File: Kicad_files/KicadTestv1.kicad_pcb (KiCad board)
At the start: 2 copper layers, 7 parts, among them J1 Conn_01x10_MountingPin, J2 Conn_01x04, SW1 SW_Push

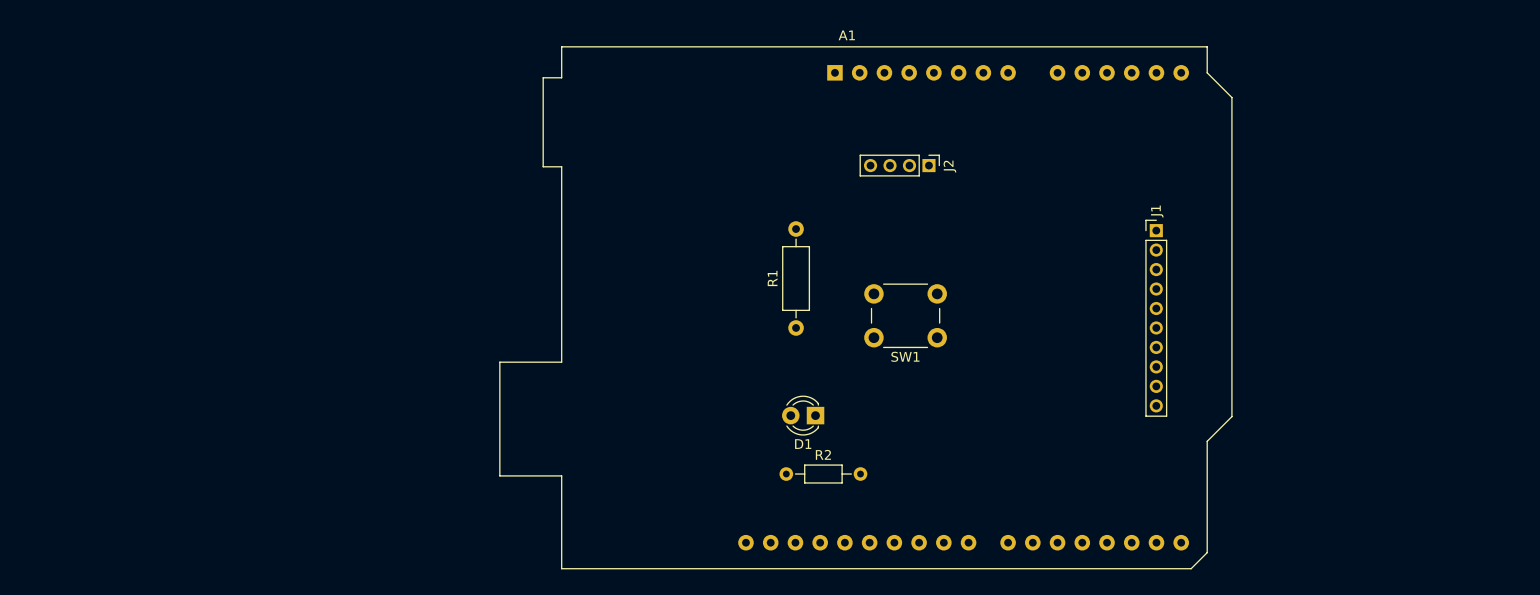
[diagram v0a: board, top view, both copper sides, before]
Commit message: Ajout Lib pour RN2483 & Modificition Empreinte et cablage
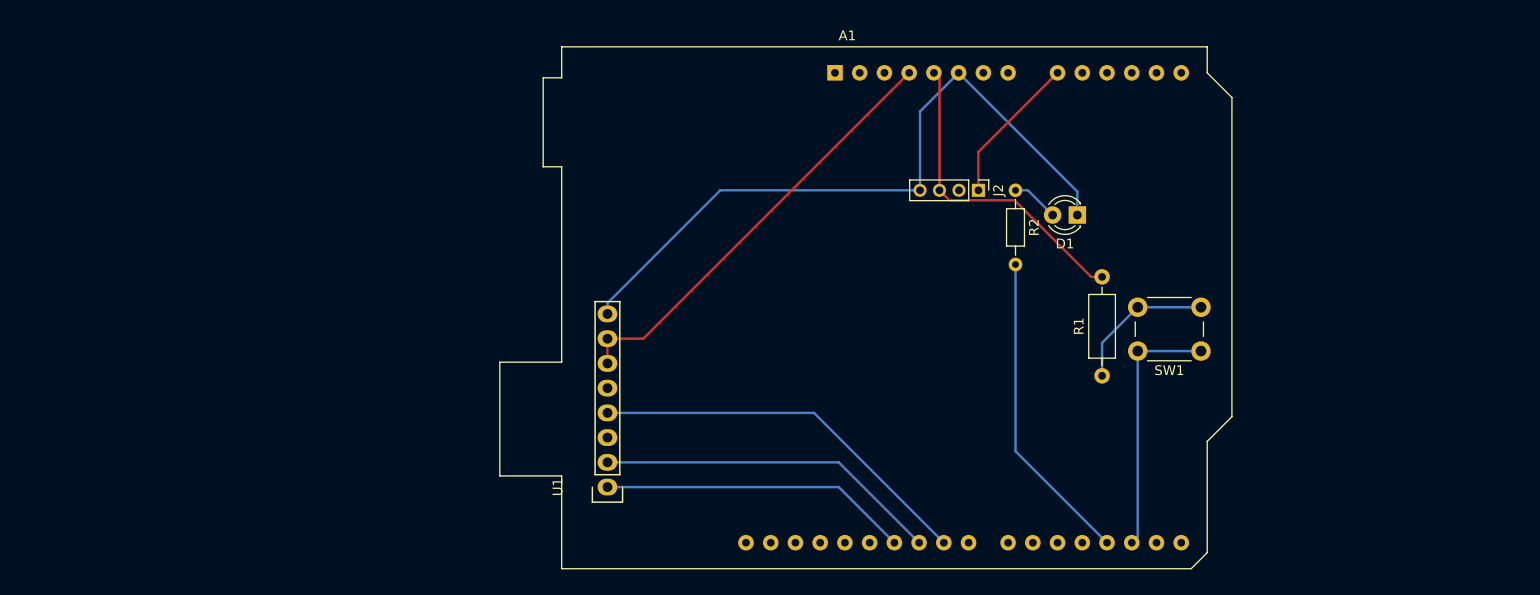
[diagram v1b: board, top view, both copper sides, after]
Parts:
- removed J1: Conn_01x10_MountingPin, Connector_PinHeader_2.00mm:PinHeader_1x10_P2.00mm_Vertical
- added U1: RN2483A, Socket_Arduino_Uno:Socket_Strip_Arduino_1x08, F.Cu at (151.1, 116.8)
- moved R2 37.5 mm to (193.0, 86.4), turned to 270 degrees
- moved D1 33.9 mm to (199.4, 88.9)
- moved R1 31.8 mm to (201.9, 105.4)
- moved SW1 27.1 mm to (212.1, 102.9)
- moved J2 5.68 mm to (189.2, 86.4)
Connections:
- A1 pad 4: Net-(A1-Pad4) -> +3V3
- A1 pad 9: Net-(A1-Pad9) -> A0
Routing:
- net GND: track 0.00 -> 71.4 mm
- net +3V3: track 0.00 -> 44.8 mm
- net RST: track 0.00 -> 40.1 mm
- net Rx: track 0.00 -> 35.4 mm
- net +5V: track 0.00 -> 32.7 mm
- net D3: track 0.00 -> 32.5 mm
- net Tx: track 0.00 -> 31.8 mm
- net D2: track 0.00 -> 26.4 mm
- net A0: track 0.00 -> 15.4 mm
- net Net-(R1-Pad1): track 0.00 -> 15.1 mm
- net Net-(D1-Pad2): track 0.00 -> 4.86 mm

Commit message: Modification empreinte et ajout circuit capteur AIME + faire routage
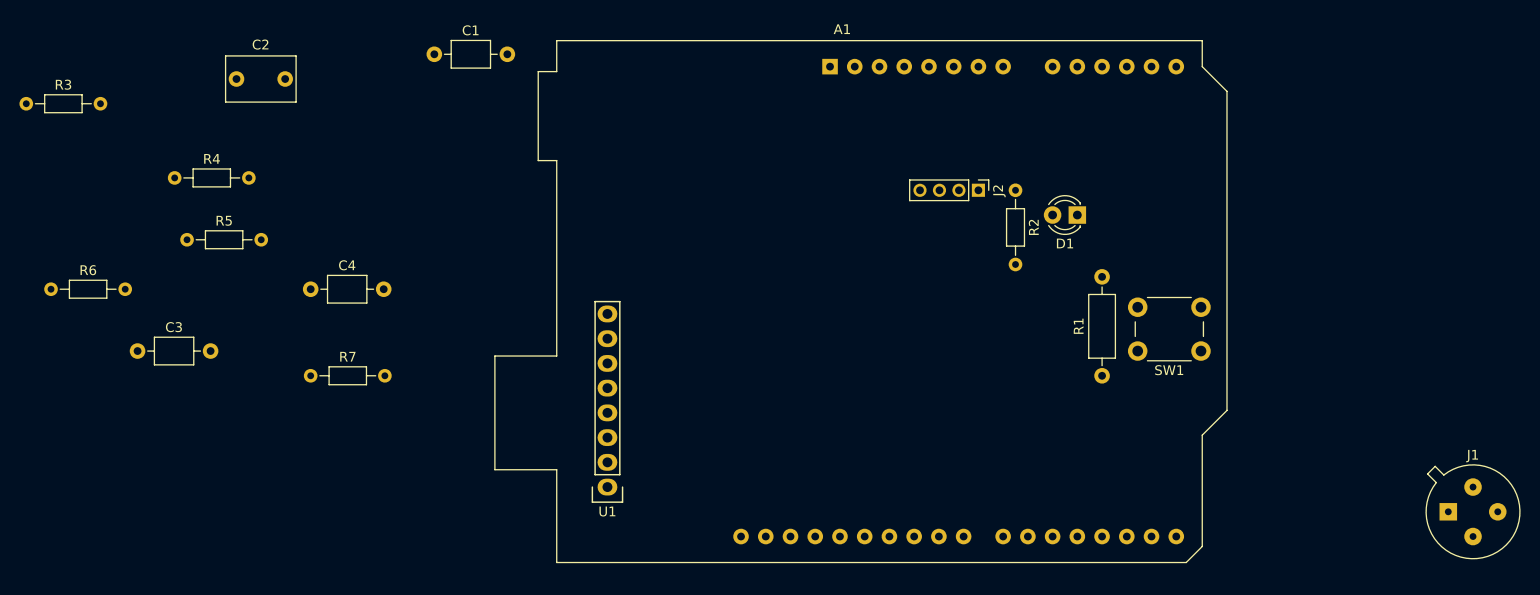
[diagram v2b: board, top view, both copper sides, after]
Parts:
- added C1: 100n, Capacitor_THT:C_Axial_L3.8mm_D2.6mm_P7.50mm_Horizontal, F.Cu at (133.3, 72.4)
- added C2: 1µ, Capacitor_THT:C_Rect_L7.0mm_W4.5mm_P5.00mm, F.Cu at (113.0, 74.9)
- added C3: 100n, Capacitor_THT:C_Axial_L3.8mm_D2.6mm_P7.50mm_Horizontal, F.Cu at (102.9, 102.9)
- added C4: 100n, Capacitor_THT:C_Axial_L3.8mm_D2.6mm_P7.50mm_Horizontal, F.Cu at (120.7, 96.5)
- added J1: Conn_01x04, ShieldArduino_Empreintes:TO-5-4_1, F.Cu at (237.5, 119.4)
- added R3: 10k, Resistor_THT:R_Axial_DIN0204_L3.6mm_D1.6mm_P7.62mm_Horizontal, F.Cu at (91.4, 77.5)
- added R4: 100k, Resistor_THT:R_Axial_DIN0204_L3.6mm_D1.6mm_P7.62mm_Horizontal, F.Cu at (106.7, 85.1)
- added R5: 1k, Resistor_THT:R_Axial_DIN0204_L3.6mm_D1.6mm_P7.62mm_Horizontal, F.Cu at (108.0, 91.4)
- added R6: 100k, Resistor_THT:R_Axial_DIN0204_L3.6mm_D1.6mm_P7.62mm_Horizontal, F.Cu at (94.0, 96.5)
- added R7: 1k, Resistor_THT:R_Axial_DIN0204_L3.6mm_D1.6mm_P7.62mm_Horizontal, F.Cu at (120.7, 105.4)
- moved A1 0.81 mm to (174.0, 73.7)
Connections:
- A1 pad 10: Net-(A1-Pad10) -> A1
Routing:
- net GND: track 71.4 -> 0.00 mm
- net +3V3: track 44.8 -> 0.00 mm
- net RST: track 40.1 -> 0.00 mm
- net Rx: track 35.4 -> 0.00 mm
- net +5V: track 32.7 -> 0.00 mm
- net D3: track 32.5 -> 0.00 mm
- net Tx: track 31.8 -> 0.00 mm
- net D2: track 26.4 -> 0.00 mm
- net A0: track 15.4 -> 0.00 mm
- net Net-(R1-Pad1): track 15.1 -> 0.00 mm
- net Net-(D1-Pad2): track 4.86 -> 0.00 mm

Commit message: Debut cablages
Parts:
- added U2: LTC1050, Package_DIP:DIP-8_W7.62mm_LongPads, F.Cu at (179.1, 100.3)
- moved R3 120.8 mm to (212.1, 82.5), turned to 180 degrees
- moved R4 101.6 mm to (208.3, 86.4), turned to 270 degrees
- moved J1 94.6 mm to (149.9, 83.8)
- moved C2 82.8 mm to (195.6, 81.3)
- moved C1 81.6 mm to (212.1, 94.0), turned to 90 degrees
- moved R6 79.0 mm to (171.4, 81.3)
- moved R5 76.9 mm to (184.2, 81.3)
- moved C3 70.5 mm to (171.4, 86.4)
- moved R7 43.7 mm to (160.0, 86.4)
- moved C4 42.2 mm to (160.0, 81.3)
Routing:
- net GND: track 0.00 -> 116.4 mm
- net +5V: track 0.00 -> 53.3 mm
- net RST: track 0.00 -> 39.3 mm
- net Rx: track 0.00 -> 34.7 mm
- net D3: track 0.00 -> 31.6 mm
- net Tx: track 0.00 -> 31.1 mm
- net D2: track 0.00 -> 26.0 mm
- net +3V3: track 0.00 -> 21.6 mm
- net Net-(C1-Pad1): track 0.00 -> 16.2 mm
- net A0: track 0.00 -> 15.9 mm
- net Net-(R1-Pad1): track 0.00 -> 15.1 mm
- net Net-(C2-Pad2): track 0.00 -> 6.66 mm
- net A1: track 0.00 -> 5.08 mm
- net Net-(D1-Pad2): track 0.00 -> 4.86 mm
- net Net-(C2-Pad1): track 0.00 -> 3.81 mm

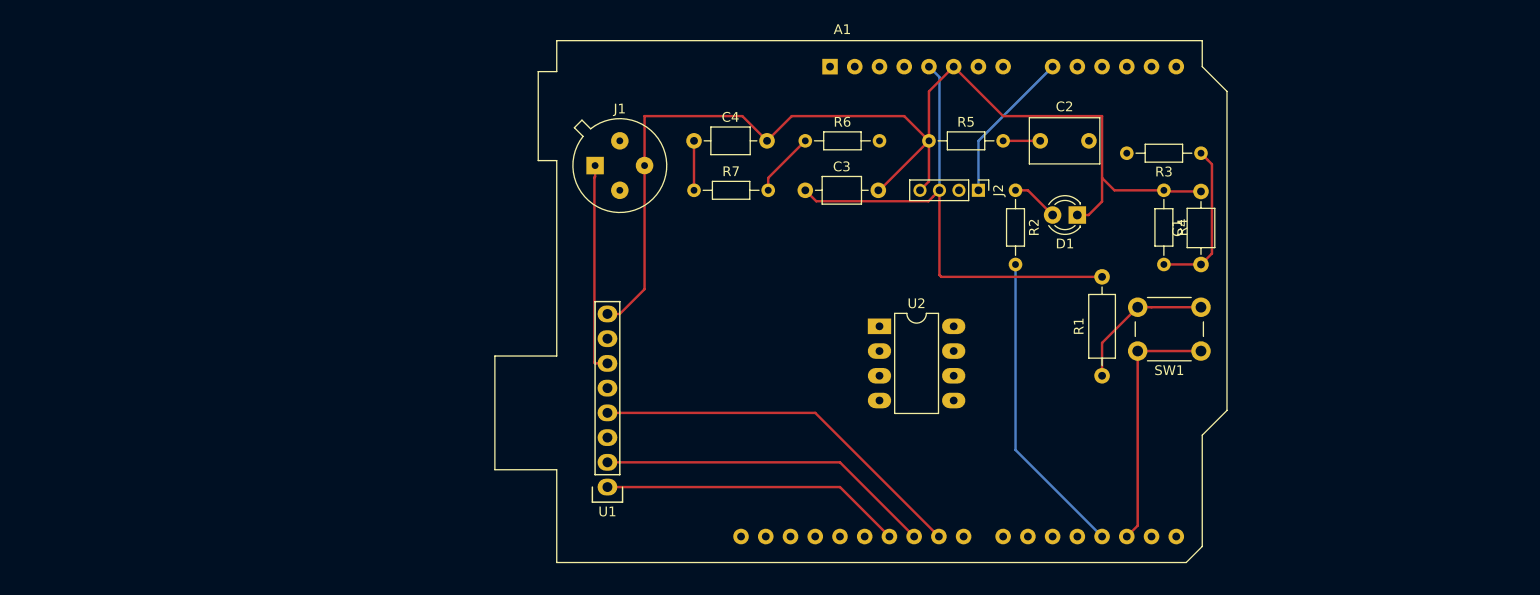
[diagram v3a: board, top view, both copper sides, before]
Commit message: Cablage fait + verifier prochain commit si le module LoRa rentre
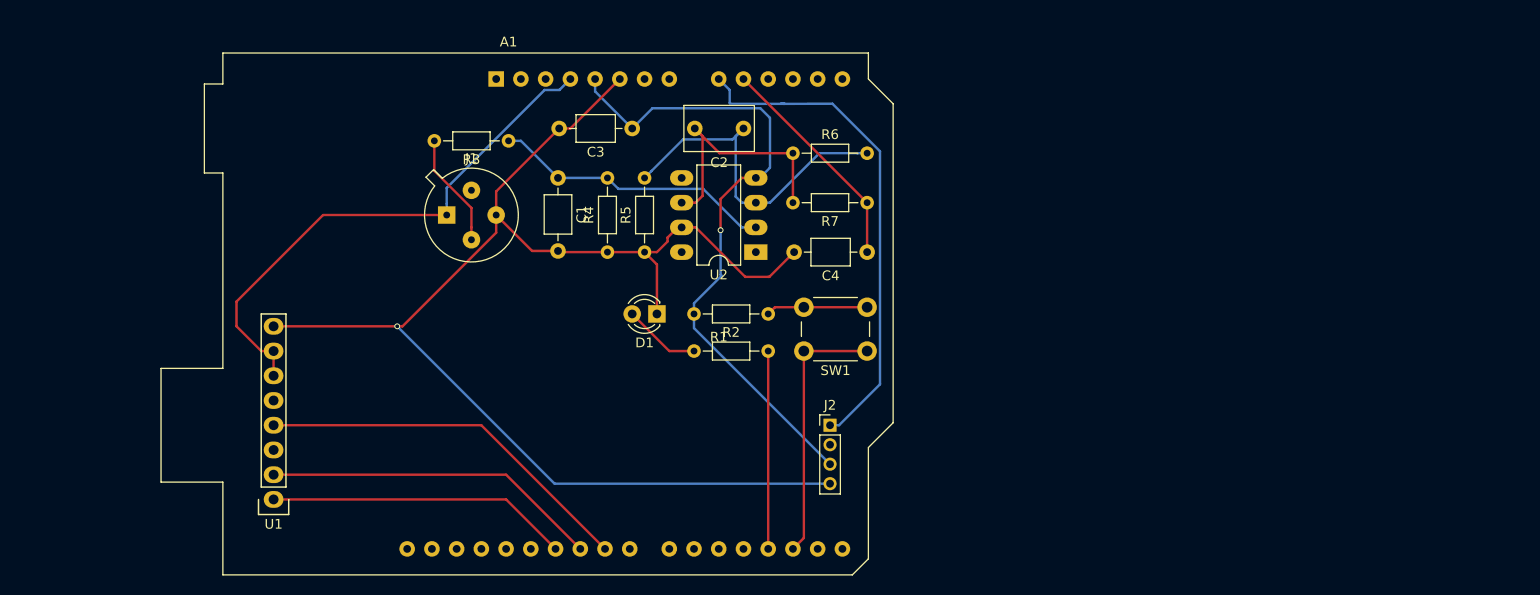
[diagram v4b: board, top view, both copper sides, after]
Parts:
- R1: footprint Resistor_THT:R_Axial_DIN0207_L6.3mm_D2.5mm_P10.16mm_Horizontal -> Resistor_THT:R_Axial_DIN0204_L3.6mm_D1.6mm_P7.62mm_Horizontal
- moved R3 71.1 mm to (141.0, 81.3)
- moved C1 66.6 mm to (146.1, 85.1), turned to 270 degrees
- moved R4 57.5 mm to (151.1, 92.7), turned to 90 degrees
- moved D1 44.4 mm to (156.2, 99.1)
- moved R2 36.9 mm to (160.0, 102.9), turned to 0 degrees
- moved R1 34.9 mm to (167.6, 99.1), turned to 180 degrees
- moved A1 34.3 mm to (139.7, 74.9)
- moved U1 34.3 mm to (116.8, 118.1)
- moved SW1 34.3 mm to (177.8, 102.9)
- moved R5 31.4 mm to (154.9, 92.7), turned to 90 degrees
- moved C2 30.5 mm to (165.1, 80.0), turned to 180 degrees
- moved J2 28.5 mm to (174.0, 110.5), turned to 0 degrees
- moved C4 21.1 mm to (177.8, 92.7), turned to 180 degrees
- moved C3 18.9 mm to (153.7, 80.0), turned to 180 degrees
- moved R7 17.8 mm to (177.8, 87.6), turned to 180 degrees
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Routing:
- net A0: track 15.9 -> 51.8 mm
- net +3V3: track 21.6 -> 55.3 mm
- net Net-(C2-Pad1): track 3.81 -> 35.5 mm
- net GND: track 116.4 -> 143.2 mm, vias 0 -> 1
- net Net-(C2-Pad2): track 6.66 -> 25.9 mm
- net A1: track 5.08 -> 23.0 mm
- net +5V: track 53.3 -> 67.8 mm, vias 0 -> 1
- net Net-(C1-Pad1): track 16.2 -> 29.1 mm
- net Net-(J1-Pad2): track 0.00 -> 11.7 mm
- net D3: track 31.6 -> 20.3 mm
- net Net-(R1-Pad1): track 15.1 -> 10.4 mm
- net Net-(D1-Pad2): track 4.86 -> 7.93 mm
- net D2: track 26.0 -> 27.3 mm
